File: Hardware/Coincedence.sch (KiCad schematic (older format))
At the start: 9 parts, among them U3 MAX991, U4 741G08

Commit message: Add power section. Switch to smaller pot
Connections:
- net labels added: +3.3V
- net labels removed: +5V
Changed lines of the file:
@@
 $Descr A4 11693 8268
 encoding utf-8
-Sheet 4 7
+Sheet 4 8
 Title "Solid State Cosmic Ray Detector"
 Date "24 sep 2013"
@@
 	1    0    0    -1
 $EndComp
-$Comp
-L +5V #PWR021
-U 1 1 523F90E7
-P 3400 2700
-F 0 "#PWR021" H 3400 2790 20  0001 C CNN
-F 1 "+5V" H 3400 2790 30  0000 C CNN
-F 2 "" H 3400 2700 60  0000 C CNN
-F 3 "" H 3400 2700 60  0000 C CNN
-	1    3400 2700
-	1    0    0    -1
-$EndComp
 Wire Wire Line
 	3400 2700 3400 2900
@@
 Connection ~ 3400 2800
 $Comp
-L GND #PWR022
+L GND #PWR22
 U 1 1 523F9103
 P 4100 2800
-F 0 "#PWR022" H 4100 2800 30  0001 C CNN
+F 0 "#PWR22" H 4100 2800 30  0001 C CNN
 F 1 "GND" H 4100 2730 30  0001 C CNN
 F 2 "" H 4100 2800 60  0000 C CNN
@@
 $EndComp
 $Comp
-L GND #PWR023
+L GND #PWR27
 U 1 1 523F9112
 P 3400 3800
-F 0 "#PWR023" H 3400 3800 30  0001 C CNN
+F 0 "#PWR27" H 3400 3800 30  0001 C CNN
 F 1 "GND" H 3400 3730 30  0001 C CNN
 F 2 "" H 3400 3800 60  0000 C CNN
@@
 	0    -1   -1   0
 $EndComp
-$Comp
-L +5V #PWR024
-U 1 1 523FBE57
-P 1900 2900
-F 0 "#PWR024" H 1900 2990 20  0001 C CNN
-F 1 "+5V" H 1900 2990 30  0000 C CNN
-F 2 "" H 1900 2900 60  0000 C CNN
-F 3 "" H 1900 2900 60  0000 C CNN
-	1    1900 2900
-	1    0    0    -1
-$EndComp
 Wire Wire Line
 	1900 2900 1900 3100
@@
 Connection ~ 1900 4500
 $Comp
-L GND #PWR025
+L GND #PWR29
 U 1 1 523FBEA8
 P 1400 5200
-F 0 "#PWR025" H 1400 5200 30  0001 C CNN
+F 0 "#PWR29" H 1400 5200 30  0001 C CNN
 F 1 "GND" H 1400 5130 30  0001 C CNN
 F 2 "" H 1400 5200 60  0000 C CNN
@@
 $EndComp
 $Comp
-L GND #PWR026
+L GND #PWR26
 U 1 1 523FBEB7
 P 1400 3700
-F 0 "#PWR026" H 1400 3700 30  0001 C CNN
+F 0 "#PWR26" H 1400 3700 30  0001 C CNN
 F 1 "GND" H 1400 3630 30  0001 C CNN
 F 2 "" H 1400 3700 60  0000 C CNN
@@
 $EndComp
 $Comp
-L GND #PWR027
+L GND #PWR30
 U 1 1 523FBEC6
 P 1900 5200
-F 0 "#PWR027" H 1900 5200 30  0001 C CNN
+F 0 "#PWR30" H 1900 5200 30  0001 C CNN
 F 1 "GND" H 1900 5130 30  0001 C CNN
 F 2 "" H 1900 5200 60  0000 C CNN
@@
 	4100 4200 4100 4900
 Connection ~ 4100 4900
-$Comp
-L +5V #PWR028
-U 1 1 523FC3F3
-P 4800 3450
-F 0 "#PWR028" H 4800 3540 20  0001 C CNN
-F 1 "+5V" H 4800 3540 30  0000 C CNN
-F 2 "" H 4800 3450 60  0000 C CNN
-F 3 "" H 4800 3450 60  0000 C CNN
-	1    4800 3450
-	1    0    0    -1
-$EndComp
 Wire Wire Line
 	4800 3450 4800 3700
@@
 Connection ~ 4800 3600
 $Comp
-L GND #PWR029
+L GND #PWR28
 U 1 1 523FC44B
 P 4800 4600
-F 0 "#PWR029" H 4800 4600 30  0001 C CNN
+F 0 "#PWR28" H 4800 4600 30  0001 C CNN
 F 1 "GND" H 4800 4530 30  0001 C CNN
 F 2 "" H 4800 4600 60  0000 C CNN
@@
 	5700 4100 5300 4100
 $Comp
-L GND #PWR030
+L GND #PWR25
 U 1 1 523FC558
 P 5500 3600
-F 0 "#PWR030" H 5500 3600 30  0001 C CNN
+F 0 "#PWR25" H 5500 3600 30  0001 C CNN
 F 1 "GND" H 5500 3530 30  0001 C CNN
 F 2 "" H 5500 3600 60  0000 C CNN
@@
 	2100 4100 2700 4100
 Connection ~ 2700 4100
+$Comp
+L +3.3V #PWR23
+U 1 1 5241F568
+P 1900 2900
+F 0 "#PWR23" H 1900 2860 30  0001 C CNN
+F 1 "+3.3V" H 1900 3010 30  0000 C CNN
+F 2 "" H 1900 2900 60  0000 C CNN
+F 3 "" H 1900 2900 60  0000 C CNN
+	1    1900 2900
+	1    0    0    -1
+$EndComp
+$Comp
+L +3.3V #PWR21
+U 1 1 5241F577
+P 3400 2700
+F 0 "#PWR21" H 3400 2660 30  0001 C CNN
+F 1 "+3.3V" H 3400 2810 30  0000 C CNN
+F 2 "" H 3400 2700 60  0000 C CNN
+F 3 "" H 3400 2700 60  0000 C CNN
+	1    3400 2700
+	1    0    0    -1
+$EndComp
+$Comp
+L +3.3V #PWR24
+U 1 1 5241F586
+P 4800 3450
+F 0 "#PWR24" H 4800 3410 30  0001 C CNN
+F 1 "+3.3V" H 4800 3560 30  0000 C CNN
+F 2 "" H 4800 3450 60  0000 C CNN
+F 3 "" H 4800 3450 60  0000 C CNN
+	1    4800 3450
+	1    0    0    -1
+$EndComp
 $EndSCHEMATC

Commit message: Associate switches
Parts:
- RV1: Distributor Part No 3361P-103GLFCT-ND -> A106089CT-ND; MFR Name Bourns -> TE; MFR Part No 3361P-1-103GLF -> 1623916-3; Power 0.5W -> 0.05W
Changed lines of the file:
@@
 Sheet 4 8
 Title "Solid State Cosmic Ray Detector"
-Date "24 sep 2013"
+Date "26 sep 2013"
 Rev "1"
 Comp "Ethan Harstad"
@@
 Connection ~ 3400 2800
 $Comp
-L GND #PWR22
+L GND #PWR021
 U 1 1 523F9103
 P 4100 2800
-F 0 "#PWR22" H 4100 2800 30  0001 C CNN
+F 0 "#PWR021" H 4100 2800 30  0001 C CNN
 F 1 "GND" H 4100 2730 30  0001 C CNN
 F 2 "" H 4100 2800 60  0000 C CNN
@@
 $EndComp
 $Comp
-L GND #PWR27
+L GND #PWR022
 U 1 1 523F9112
 P 3400 3800
-F 0 "#PWR27" H 3400 3800 30  0001 C CNN
+F 0 "#PWR022" H 3400 3800 30  0001 C CNN
 F 1 "GND" H 3400 3730 30  0001 C CNN
 F 2 "" H 3400 3800 60  0000 C CNN
@@
 F 2 "POT-3361P" H 1900 4100 60  0001 C CNN
 F 3 "~" H 1900 4100 60  0000 C CNN
-F 4 "Bourns" H 1900 4100 60  0001 C CNN "MFR Name"
-F 5 "3361P-1-103GLF" H 1900 4100 60  0001 C CNN "MFR Part No"
-F 6 "3361P-103GLFCT-ND" H 1900 4100 60  0001 C CNN "Distributor Part No"
-F 7 "0.5W" H 1950 4000 50  0001 L CNN "Power"
+F 4 "TE" H 1900 4100 60  0001 C CNN "MFR Name"
+F 5 "1623916-3" H 1900 4100 60  0001 C CNN "MFR Part No"
+F 6 "A106089CT-ND" H 1900 4100 60  0001 C CNN "Distributor Part No"
+F 7 "0.05W" H 1950 4000 50  0001 L CNN "Power"
 F 8 "10%" H 1850 4000 50  0001 R CNN "Tolerance"
 	1    1900 4100
@@
 Connection ~ 1900 4500
 $Comp
-L GND #PWR29
+L GND #PWR023
 U 1 1 523FBEA8
 P 1400 5200
-F 0 "#PWR29" H 1400 5200 30  0001 C CNN
+F 0 "#PWR023" H 1400 5200 30  0001 C CNN
 F 1 "GND" H 1400 5130 30  0001 C CNN
 F 2 "" H 1400 5200 60  0000 C CNN
@@
 $EndComp
 $Comp
-L GND #PWR26
+L GND #PWR024
 U 1 1 523FBEB7
 P 1400 3700
-F 0 "#PWR26" H 1400 3700 30  0001 C CNN
+F 0 "#PWR024" H 1400 3700 30  0001 C CNN
 F 1 "GND" H 1400 3630 30  0001 C CNN
 F 2 "" H 1400 3700 60  0000 C CNN
@@
 $EndComp
 $Comp
-L GND #PWR30
+L GND #PWR025
 U 1 1 523FBEC6
 P 1900 5200
-F 0 "#PWR30" H 1900 5200 30  0001 C CNN
+F 0 "#PWR025" H 1900 5200 30  0001 C CNN
 F 1 "GND" H 1900 5130 30  0001 C CNN
 F 2 "" H 1900 5200 60  0000 C CNN
@@
 Connection ~ 4800 3600
 $Comp
-L GND #PWR28
+L GND #PWR026
 U 1 1 523FC44B
 P 4800 4600
-F 0 "#PWR28" H 4800 4600 30  0001 C CNN
+F 0 "#PWR026" H 4800 4600 30  0001 C CNN
 F 1 "GND" H 4800 4530 30  0001 C CNN
 F 2 "" H 4800 4600 60  0000 C CNN
@@
 	5700 4100 5300 4100
 $Comp
-L GND #PWR25
+L GND #PWR027
 U 1 1 523FC558
 P 5500 3600
-F 0 "#PWR25" H 5500 3600 30  0001 C CNN
+F 0 "#PWR027" H 5500 3600 30  0001 C CNN
 F 1 "GND" H 5500 3530 30  0001 C CNN
 F 2 "" H 5500 3600 60  0000 C CNN
@@
 Connection ~ 2700 4100
 $Comp
-L +3.3V #PWR23
+L +3.3V #PWR028
 U 1 1 5241F568
 P 1900 2900
-F 0 "#PWR23" H 1900 2860 30  0001 C CNN
+F 0 "#PWR028" H 1900 2860 30  0001 C CNN
 F 1 "+3.3V" H 1900 3010 30  0000 C CNN
 F 2 "" H 1900 2900 60  0000 C CNN
@@
 $EndComp
 $Comp
-L +3.3V #PWR21
+L +3.3V #PWR029
 U 1 1 5241F577
 P 3400 2700
-F 0 "#PWR21" H 3400 2660 30  0001 C CNN
+F 0 "#PWR029" H 3400 2660 30  0001 C CNN
 F 1 "+3.3V" H 3400 2810 30  0000 C CNN
 F 2 "" H 3400 2700 60  0000 C CNN
@@
 $EndComp
 $Comp
-L +3.3V #PWR24
+L +3.3V #PWR030
 U 1 1 5241F586
 P 4800 3450
-F 0 "#PWR24" H 4800 3410 30  0001 C CNN
+F 0 "#PWR030" H 4800 3410 30  0001 C CNN
 F 1 "+3.3V" H 4800 3560 30  0000 C CNN
 F 2 "" H 4800 3450 60  0000 C CNN

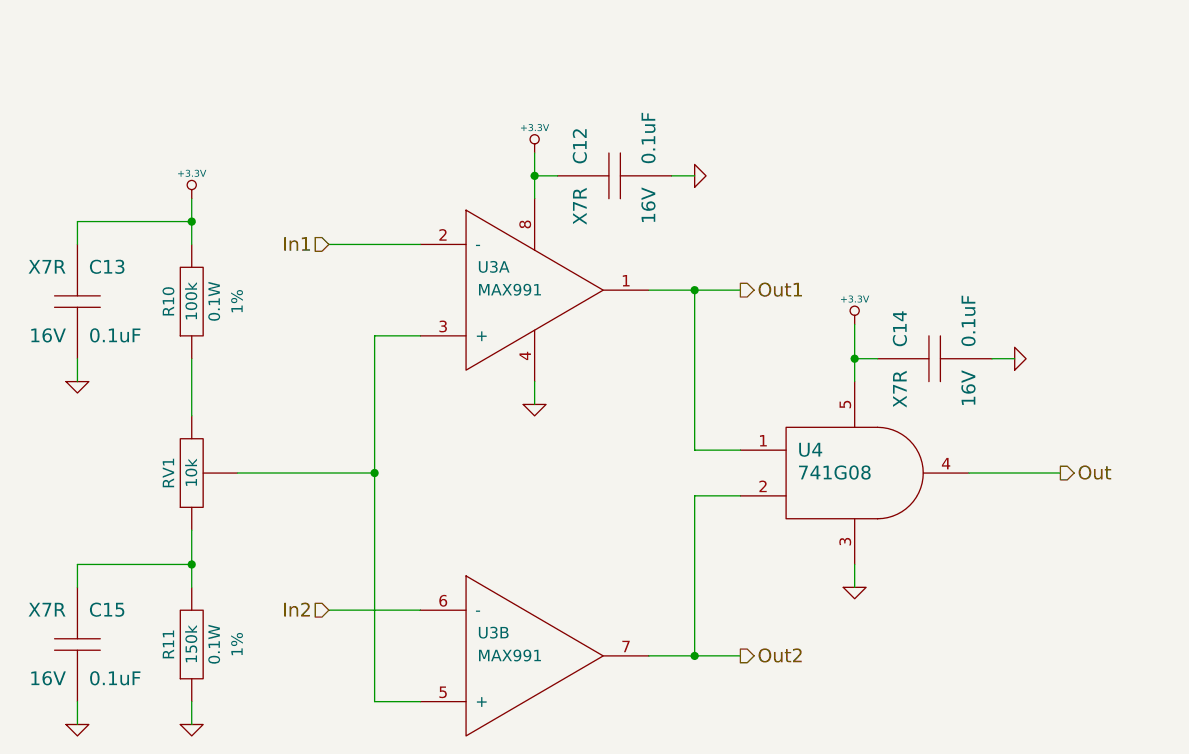
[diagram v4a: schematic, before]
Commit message: Switch to 44 pin PIC
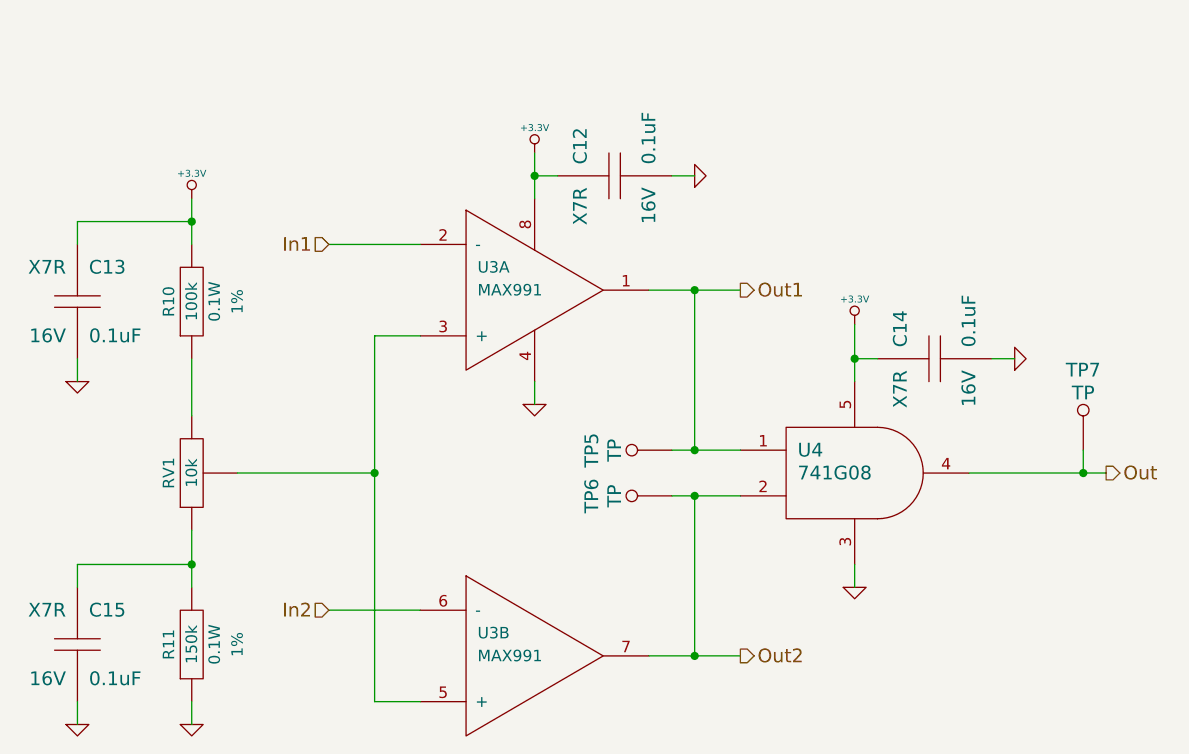
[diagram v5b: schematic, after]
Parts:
- added TP5, TP6, TP7: TP, ~, symbol TP
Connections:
- net Out: now also TP7.1
- net Out1: now also TP5.1
- net Out2: now also TP6.1
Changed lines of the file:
@@
 Sheet 4 8
 Title "Solid State Cosmic Ray Detector"
-Date "8 dec 2013"
+Date "20 dec 2013"
 Rev "1"
 Comp "Ethan Harstad"
@@
 Text HLabel 4300 4900 2    60   Output ~ 0
 Out2
-Text HLabel 5700 4100 2    60   Output ~ 0
+Text HLabel 5900 4100 2    60   Output ~ 0
 Out
 $Comp
@@
 $EndComp
 Wire Wire Line
-	4300 4000 4100 4000
+	4000 4000 4300 4000
 Wire Wire Line
 	4100 4000 4100 3300
 Connection ~ 4100 3300
 Wire Wire Line
-	4300 4200 4100 4200
+	4000 4200 4300 4200
 Wire Wire Line
 	4100 4200 4100 4900
@@
 	4800 4600 4800 4500
 Wire Wire Line
-	5700 4100 5300 4100
+	5900 4100 5300 4100
 $Comp
 L GND #PWR027
@@
 	1    0    0    -1
 $EndComp
+$Comp
+L TP TP5
+U 1 1 52B35063
+P 4000 4000
+F 0 "TP5" H 4000 4350 60  0000 C CNN
+F 1 "TP" H 4000 4250 60  0000 C CNN
+F 2 "~" H 4000 4000 60  0000 C CNN
+F 3 "~" H 4000 4000 60  0000 C CNN
+	1    4000 4000
+	0    -1   -1   0
+$EndComp
+$Comp
+L TP TP6
+U 1 1 52B35072
+P 4000 4200
+F 0 "TP6" H 4000 4550 60  0000 C CNN
+F 1 "TP" H 4000 4450 60  0000 C CNN
+F 2 "~" H 4000 4200 60  0000 C CNN
+F 3 "~" H 4000 4200 60  0000 C CNN
+	1    4000 4200
+	0    -1   -1   0
+$EndComp
+Connection ~ 4100 4000
+Connection ~ 4100 4200
+$Comp
+L TP TP7
+U 1 1 52B352B0
+P 5800 4000
+F 0 "TP7" H 5800 4350 60  0000 C CNN
+F 1 "TP" H 5800 4250 60  0000 C CNN
+F 2 "~" H 5800 4000 60  0000 C CNN
+F 3 "~" H 5800 4000 60  0000 C CNN
+	1    5800 4000
+	1    0    0    -1
+$EndComp
+Wire Wire Line
+	5800 4000 5800 4100
+Connection ~ 5800 4100
 $EndSCHEMATC
